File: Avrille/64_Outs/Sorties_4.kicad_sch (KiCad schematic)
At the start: 49 parts, among them Q18 TIP127, Q19 TIP127, Q2 TIP127, Q50 TIP127, Q51 TIP127, Q52 TIP127, Q53 TIP127, Q79 TIP127, U44 ULN2803A

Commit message: reset
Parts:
- removed D11, D121, D122, D123, D124, D152, D48, D49: 1N4002, Diode_THT:D_DO-41_SOD81_P10.16mm_Horizontal, symbol Diode:1N4002
- removed D12, D125, D126, D128, D129, D50, D51: LED, LED_SMD:LED_PLCC-2_3.4x3.0mm_AK, symbol Device:LED_Small
- removed Q18, Q19, Q2, Q50, Q51, Q52, Q53, Q79: TIP127, Package_TO_SOT_THT:TO-220-3_Vertical, symbol Transistor_BJT:TIP127
- removed R18, R195, R196, R197, R199, R77, R79: 3,9k, Resistor_THT:R_Axial_DIN0207_L6.3mm_D2.5mm_P10.16mm_Horizontal, symbol Device:R_US
- removed R19, R20, R200, R201, R203, R204, R205, R207, R208, R209, R80, R81, R82, R83: 2,2k, Resistor_THT:R_Axial_DIN0207_L6.3mm_D2.5mm_P10.16mm_Horizontal, symbol Device:R_US
- removed U44: ULN2803A, symbol Transistor_Array:ULN2803A
- added D115, D116, D117, D118: 1N4004, Diode_THT:D_DO-41_SOD81_P10.16mm_Horizontal, symbol Diode:1N4004
- added D120, D121, D122: LED, LED_THT:LED_D1.8mm_W3.3mm_H2.4mm, symbol Device:LED_Small
- added Q54, Q55, Q56, Q57: IRF9Z34, Package_TO_SOT_THT:TO-220-3_Vertical, symbol Transistor_FET:IRF4905
- added R231, R232, R233: 20k, Resistor_THT:R_Axial_DIN0207_L6.3mm_D2.5mm_P10.16mm_Horizontal, symbol Device:R_US
- added R235, R236, R237: 10k, Resistor_THT:R_Axial_DIN0207_L6.3mm_D2.5mm_P10.16mm_Horizontal, symbol Device:R_US
- added R239, R240, R241: 2,4k, Resistor_THT:R_Axial_DIN0207_L6.3mm_D2.5mm_P10.16mm_Horizontal, symbol Device:R_US
- added U27: LTV-847M, Package_DIP:DIP-16_W7.62mm, symbol Isolator:LTV-847M
- D119: footprint LED_SMD:LED_PLCC-2_3.4x3.0mm_AK -> LED_THT:LED_D1.8mm_W3.3mm_H2.4mm
- R230: value 3,9k -> 20k
- R234: value 2,2k -> 10k
- R238: value 2,2k -> 2,4k
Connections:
- net IN_1: now also U27.7
- net IN_2: now also U27.5
- net IN_3: now also U27.3
- net IN_4: now also U27.1
- net OUT_1: now also D115.1 (K), Q54.2 (D)
- net OUT_2: now also D116.1 (K), Q55.2 (D), R239.1
- net OUT_3: now also D117.1 (K), Q56.2 (D), R240.1
- net V_COM: now also D115.2 (A), D116.2 (A), D117.2 (A), D118.2 (A), D120.1 (K), D121.1 (K), D122.1 (K), U27.11, U27.13, U27.15, U27.2, U27.4, U27.6, U27.8, U27.9
- net V_IN: now also Q54.3 (S), Q55.3 (S), Q56.3 (S), Q57.3 (S), R235.1, R236.1, R237.1
- net at R230.1, R234.2: now also Q54.1 (G)
- net Cmd_1: no longer names the net of R230.2
- net Cmd_1: now also U27.16
- new net: Q57.1 (G), R233.1, R237.2
- new net: D122.2 (A), R241.2
- new net: R231.2, U27.14
- new net: Q56.1 (G), R232.1, R236.2
- new net: D121.2 (A), R240.2
- new net: R233.2, U27.10
- new net: D120.2 (A), R239.2
- new net: R232.2, U27.12
- new net: Q55.1 (G), R231.1, R235.2
- new net OUT_4: D118.1 (K), Q57.2 (D), R241.1
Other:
- note added: "60V - 18A"
- moved on the sheet: D119, R230, R234, R238

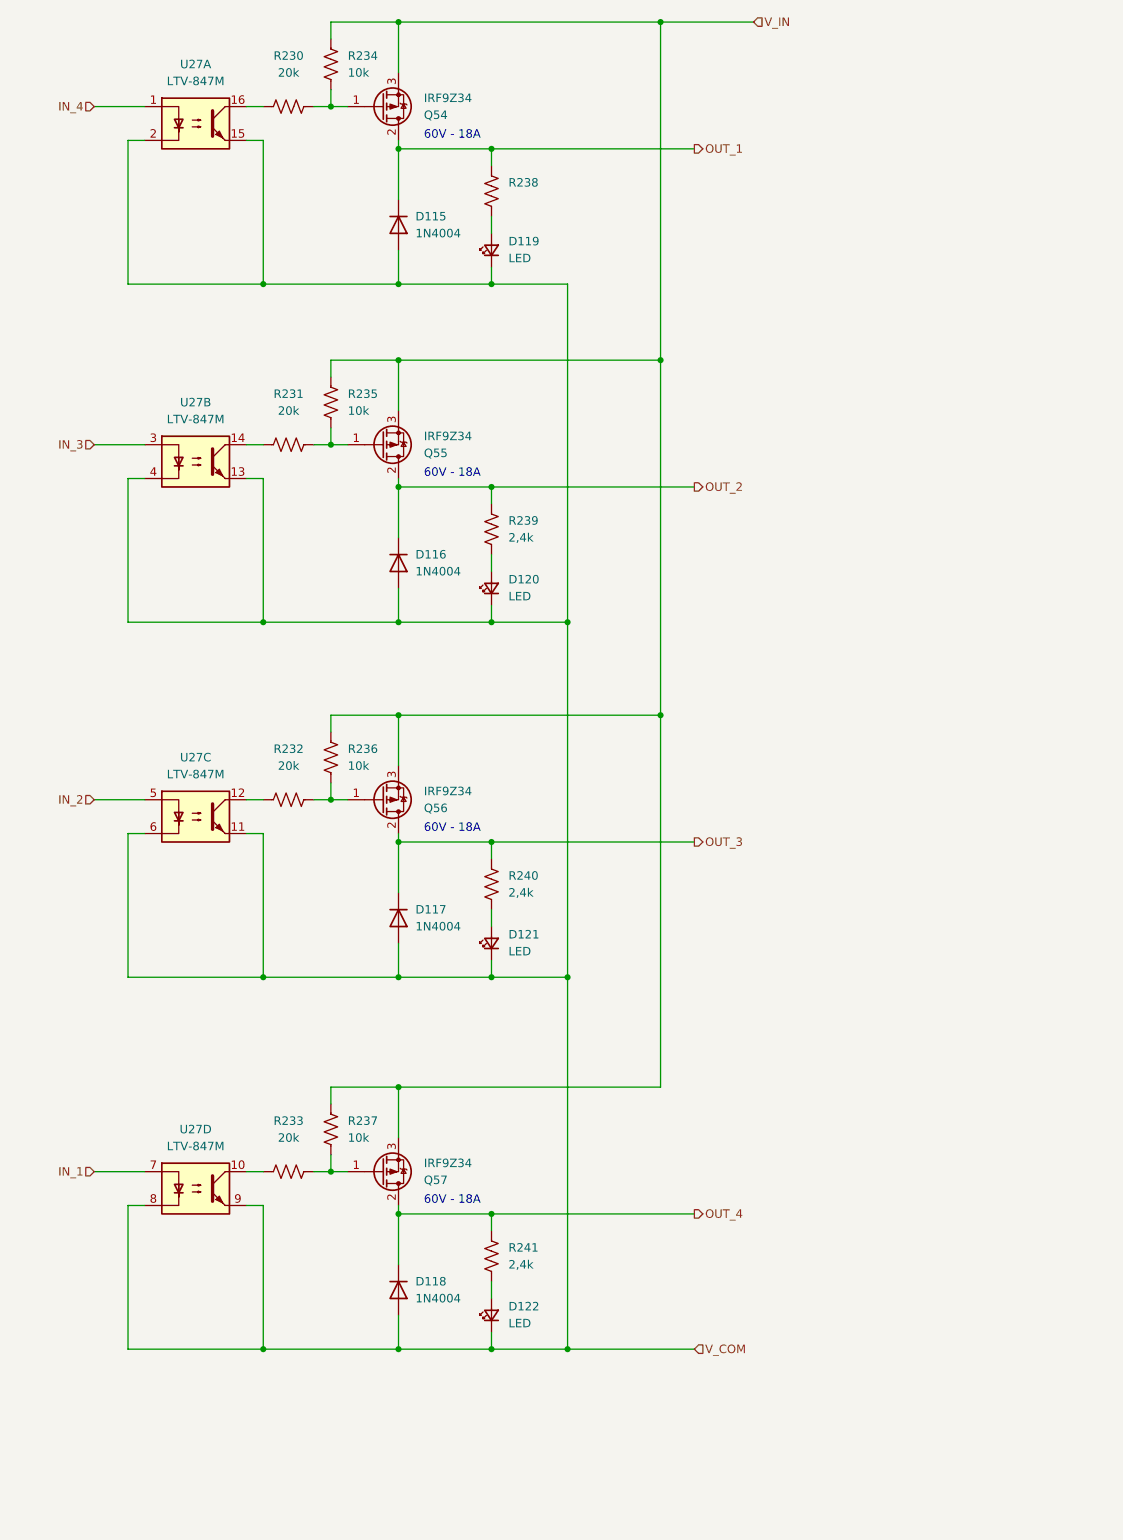
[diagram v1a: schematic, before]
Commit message: Update to SMD Version
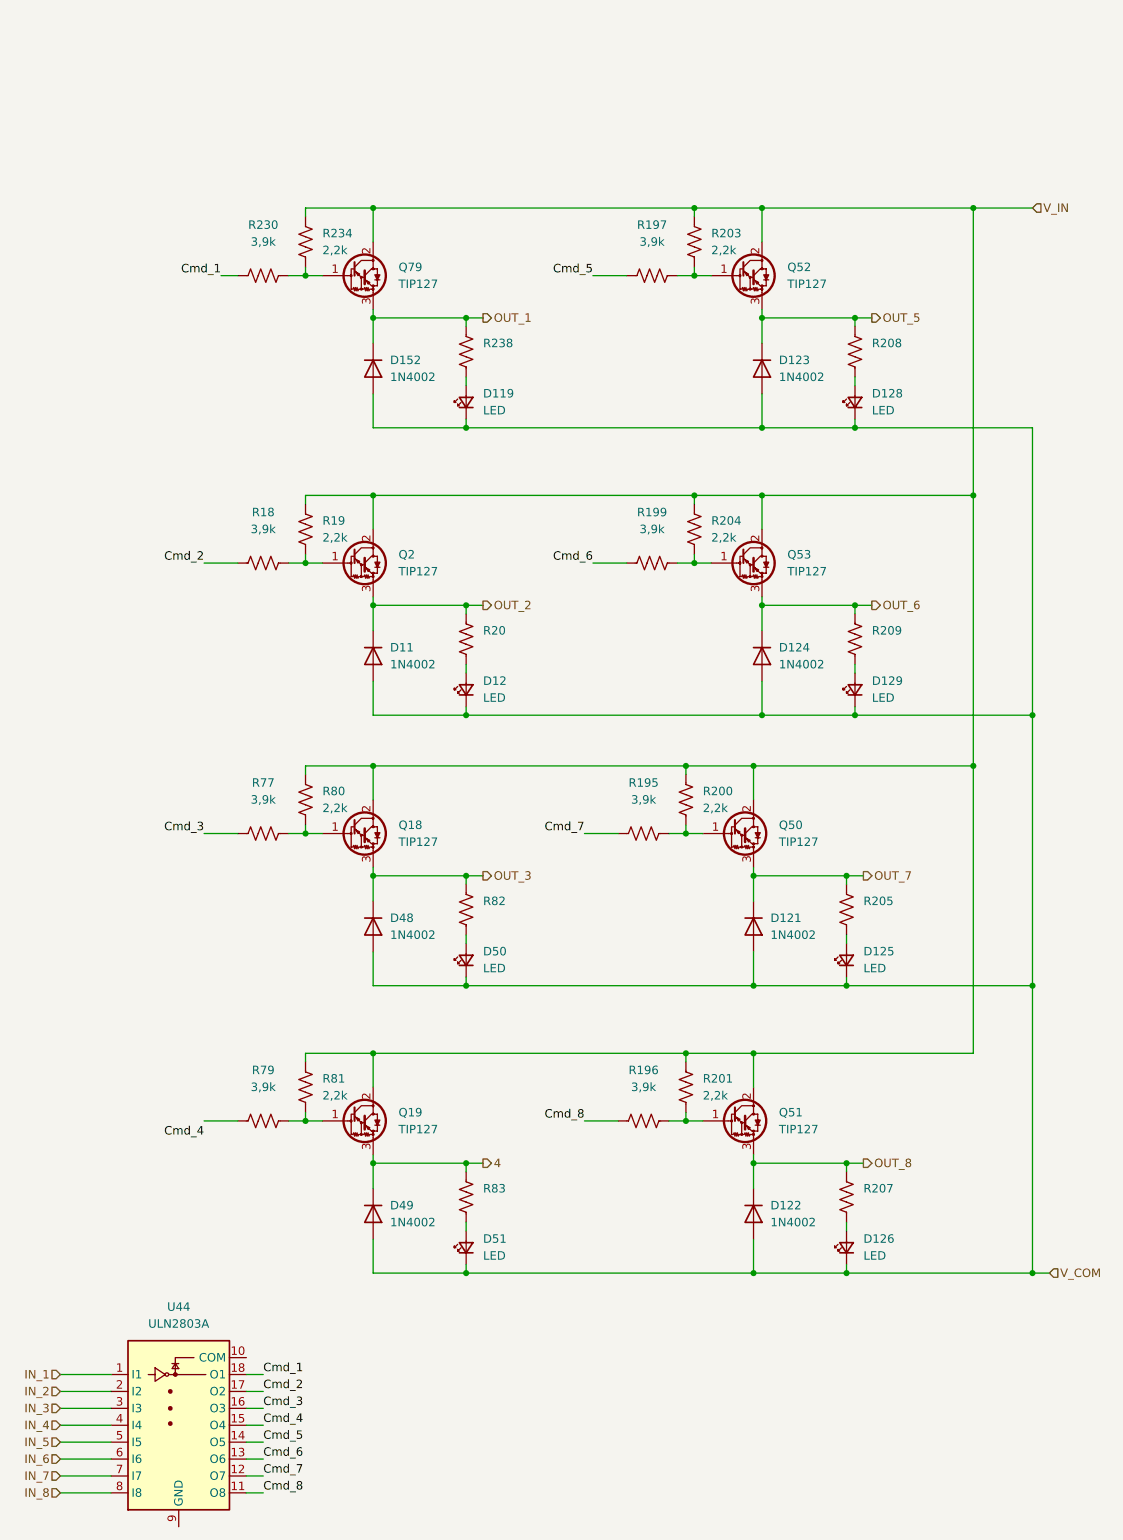
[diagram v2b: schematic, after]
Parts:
- removed D115, D116, D117, D118: 1N4004, Diode_THT:D_DO-41_SOD81_P10.16mm_Horizontal, symbol Diode:1N4004
- removed D120, D121, D122: LED, LED_THT:LED_D1.8mm_W3.3mm_H2.4mm, symbol Device:LED_Small
- removed Q54, Q55, Q56, Q57: IRF9Z34, Package_TO_SOT_THT:TO-220-3_Vertical, symbol Transistor_FET:IRF4905
- removed R231, R232, R233: 20k, Resistor_THT:R_Axial_DIN0207_L6.3mm_D2.5mm_P10.16mm_Horizontal, symbol Device:R_US
- removed R235, R236, R237: 10k, Resistor_THT:R_Axial_DIN0207_L6.3mm_D2.5mm_P10.16mm_Horizontal, symbol Device:R_US
- removed R239, R240, R241: 2,4k, Resistor_THT:R_Axial_DIN0207_L6.3mm_D2.5mm_P10.16mm_Horizontal, symbol Device:R_US
- removed U27: LTV-847M, Package_DIP:DIP-16_W7.62mm, symbol Isolator:LTV-847M
- added D11, D121, D122, D123, D124, D152, D48, D49: 1N4002, Diode_THT:D_DO-41_SOD81_P10.16mm_Horizontal, symbol Diode:1N4002
- added D12, D125, D126, D128, D129, D50, D51: LED, LED_SMD:LED_PLCC-2_3.4x3.0mm_AK, symbol Device:LED_Small
- added Q18, Q19, Q2, Q50, Q51, Q52, Q53, Q79: TIP127, Package_TO_SOT_THT:TO-220-3_Vertical, symbol Transistor_BJT:TIP127
- added R18, R195, R196, R197, R199, R77, R79: 3,9k, Resistor_THT:R_Axial_DIN0207_L6.3mm_D2.5mm_P10.16mm_Horizontal, symbol Device:R_US
- added R19, R20, R200, R201, R203, R204, R205, R207, R208, R209, R80, R81, R82, R83: 2,2k, Resistor_THT:R_Axial_DIN0207_L6.3mm_D2.5mm_P10.16mm_Horizontal, symbol Device:R_US
- added U44: ULN2803A, symbol Transistor_Array:ULN2803A
- D119: footprint LED_THT:LED_D1.8mm_W3.3mm_H2.4mm -> LED_SMD:LED_PLCC-2_3.4x3.0mm_AK
- R230: value 20k -> 3,9k
- R234: value 10k -> 2,2k
- R238: value 2,4k -> 2,2k
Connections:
- net IN_1: now also U44.1 (I1)
- net IN_2: now also U44.2 (I2)
- net IN_3: now also U44.3 (I3)
- net IN_4: now also U44.4 (I4)
- net OUT_1: now also D152.1 (K), Q79.3 (E)
- net OUT_2: now also D11.1 (K), Q2.3 (E), R20.1
- net OUT_3: now also D48.1 (K), Q18.3 (E), R82.1
- net V_COM: now also D11.2 (A), D12.1 (K), D121.2 (A), D122.2 (A), D123.2 (A), D124.2 (A), D125.1 (K), D126.1 (K), D128.1 (K), D129.1 (K), D152.2 (A), D48.2 (A), D49.2 (A), D50.1 (K), D51.1 (K)
- net V_IN: now also Q18.2 (C), Q19.2 (C), Q2.2 (C), Q50.2 (C), Q51.2 (C), Q52.2 (C), Q53.2 (C), Q79.2 (C), R19.1, R200.1, R201.1, R203.1, R204.1, R80.1, R81.1
- net Cmd_1: now reaches R230.2
- net Cmd_1: now also U44.18 (O1)
- net at R230.1, R234.2: now also Q79.1 (B)
- new net: Q51.1 (B), R196.1, R201.2
- new net: D129.2 (A), R209.2
- new net: Q2.1 (B), R18.1, R19.2
- new net: D51.2 (A), R83.2
- new net: Q50.1 (B), R195.1, R200.2
- new net: D128.2 (A), R208.2
- new net: D126.2 (A), R207.2
- new net: D12.2 (A), R20.2
- new net: Q53.1 (B), R199.1, R204.2
- new net: Q52.1 (B), R197.1, R203.2
- new net: Q19.1 (B), R79.1, R81.2
- new net: D50.2 (A), R82.2
- new net: Q18.1 (B), R77.1, R80.2
- new net: D125.2 (A), R205.2
- new net 4: D49.1 (K), Q19.3 (E), R83.1
- new net Cmd_2: R18.2, U44.17 (O2)
- new net Cmd_3: R77.2, U44.16 (O3)
- new net Cmd_4: U44.15 (O4)
- new net Cmd_5: R197.2, U44.14 (O5)
- new net Cmd_6: R199.2, U44.13 (O6)
- new net Cmd_7: R195.2, U44.12 (O7)
- new net Cmd_8: R196.2, U44.11 (O8)
- new net IN_5: U44.5 (I5)
- new net IN_6: U44.6 (I6)
- new net IN_7: U44.7 (I7)
- new net IN_8: U44.8 (I8)
- new net OUT_5: D123.1 (K), Q52.3 (E), R208.1
- new net OUT_6: D124.1 (K), Q53.3 (E), R209.1
- new net OUT_7: D121.1 (K), Q50.3 (E), R205.1
- new net OUT_8: D122.1 (K), Q51.3 (E), R207.1
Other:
- note removed: "60V - 18A"
- moved on the sheet: D119, R230, R234, R238
